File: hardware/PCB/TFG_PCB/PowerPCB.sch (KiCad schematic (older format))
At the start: 52 parts, among them J1 Conn_01x02_Male, J11 Conn_01x02_Male, J13 Conn_01x02_Male, J15 Conn_01x04_Male, J18 Conn_01x02_Male, J19 Conn_01x02_Male, J21 Conn_01x02_Male, J22 Conn_01x02_Male, J23 Conn_01x04_Male, J25 Conn_01x04_Male, J26 Conn_01x04_Male, J28 Conn_01x02_Male, J30 Conn_01x02_Male, J4 Conn_01x04_Male, J6 Conn_01x04_Male, J7 Conn_01x02_Male, J9 Conn_01x04_Male, Q1 IRF540N, Q4 FDD6685, Q6 FDD6685, Q8 2N7002, U2 L78L05_SOT89, U4 TD7590_2, U6 TD7590_2

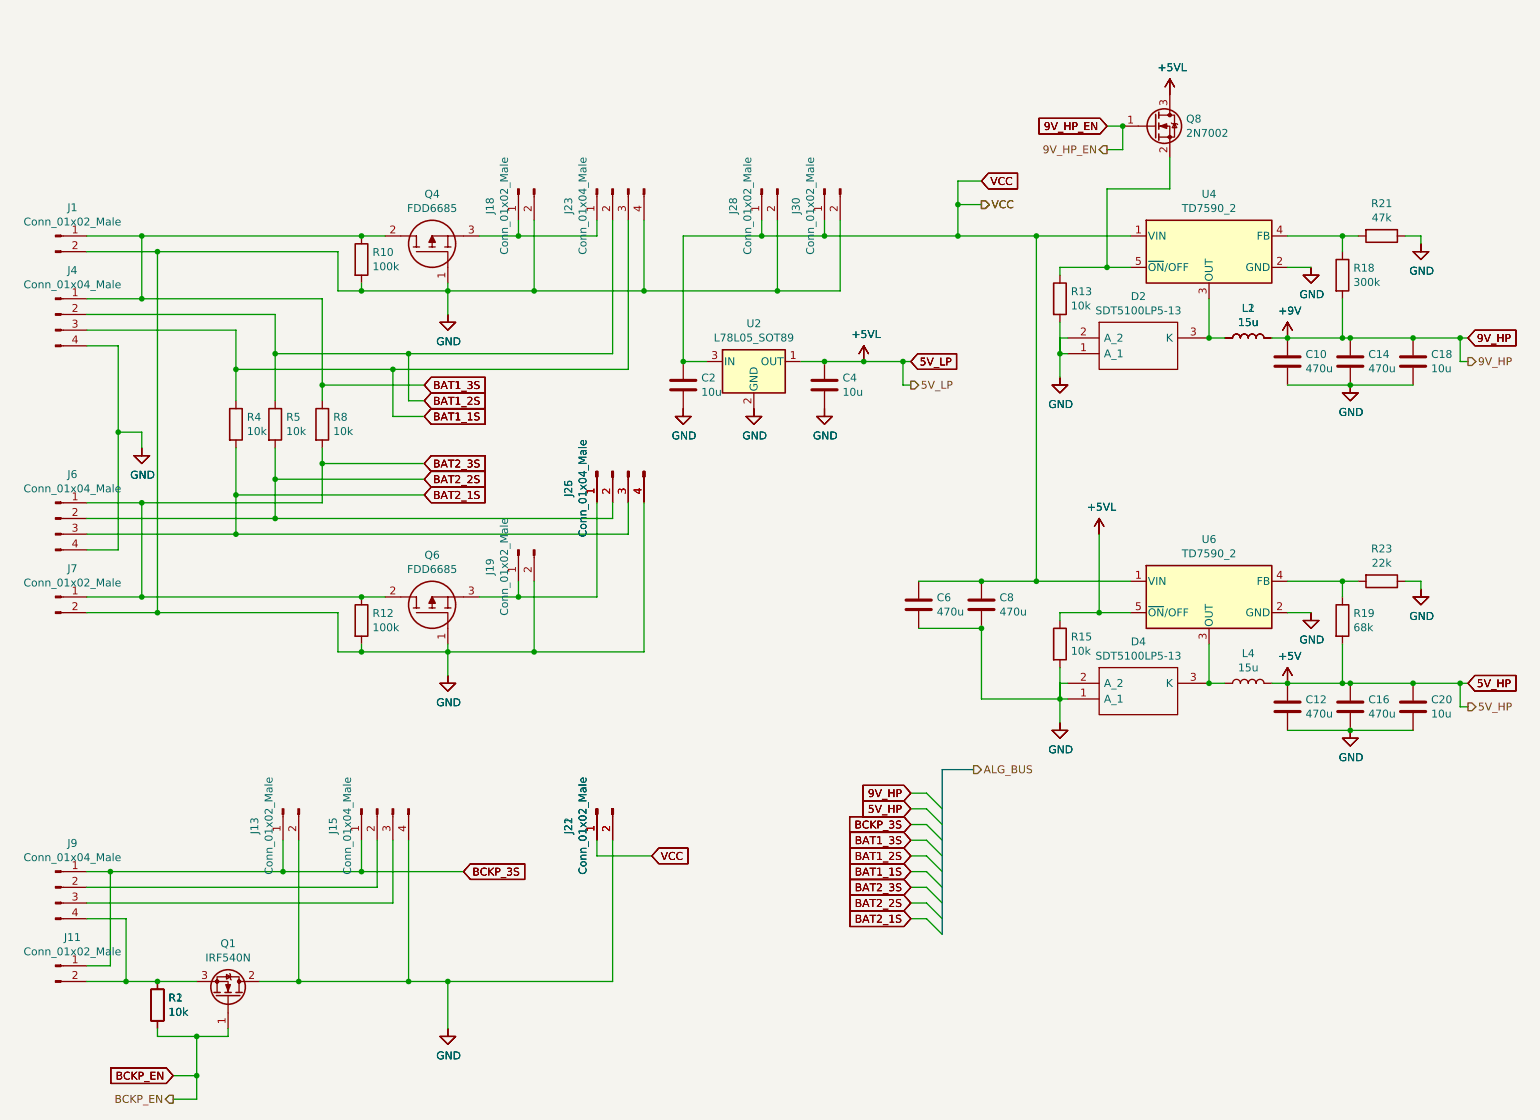
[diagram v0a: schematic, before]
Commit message: added footprints
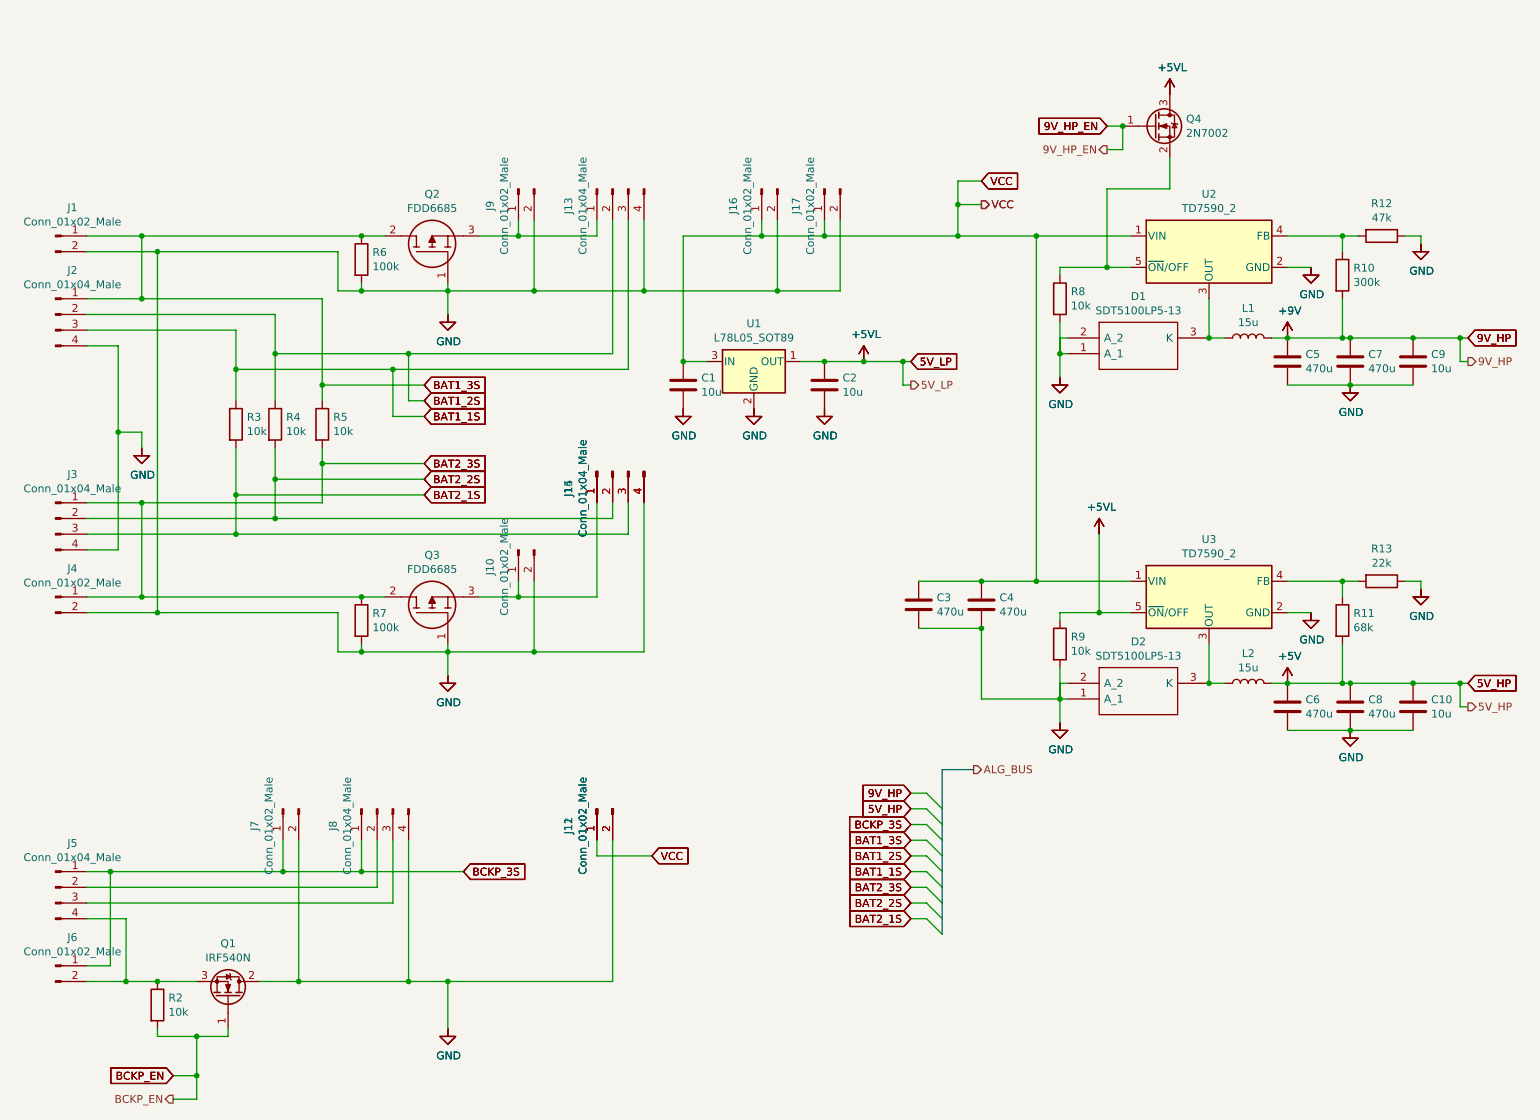
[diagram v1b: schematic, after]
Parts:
- removed L1: 15u, Inductor_SMD:L_0603_1608Metric, symbol Device:L
- removed R1: 10k, symbol Device:R
- C1: renamed from C2; footprint (none) -> Capacitor_SMD:C_2512_6332Metric_Pad1.52x3.35mm_HandSolder
- C2: renamed from C4; footprint (none) -> Capacitor_SMD:C_2512_6332Metric_Pad1.52x3.35mm_HandSolder
- renumbered C20 to C10, C6 to C3, C8 to C4, C10 to C5, C12 to C6, C14 to C7, C16 to C8, C18 to C9, D2 to D1, D4 to D2, J19 to J10, J21 to J11, J22 to J12, J23 to J13, J25 to J14, J26 to J15, J28 to J16, J30 to J17, J4 to J2, J6 to J3, J7 to J4, J9 to J5, J11 to J6, J13 to J7, J15 to J8, J18 to J9, L2 to L1, L4 to L2, Q4 to Q2, Q6 to Q3, Q8 to Q4, R18 to R10, R19 to R11, R21 to R12, R23 to R13, R4 to R3, R5 to R4, R8 to R5, R10 to R6, R12 to R7, R13 to R8, R15 to R9, U2 to U1, U4 to U2, U6 to U3

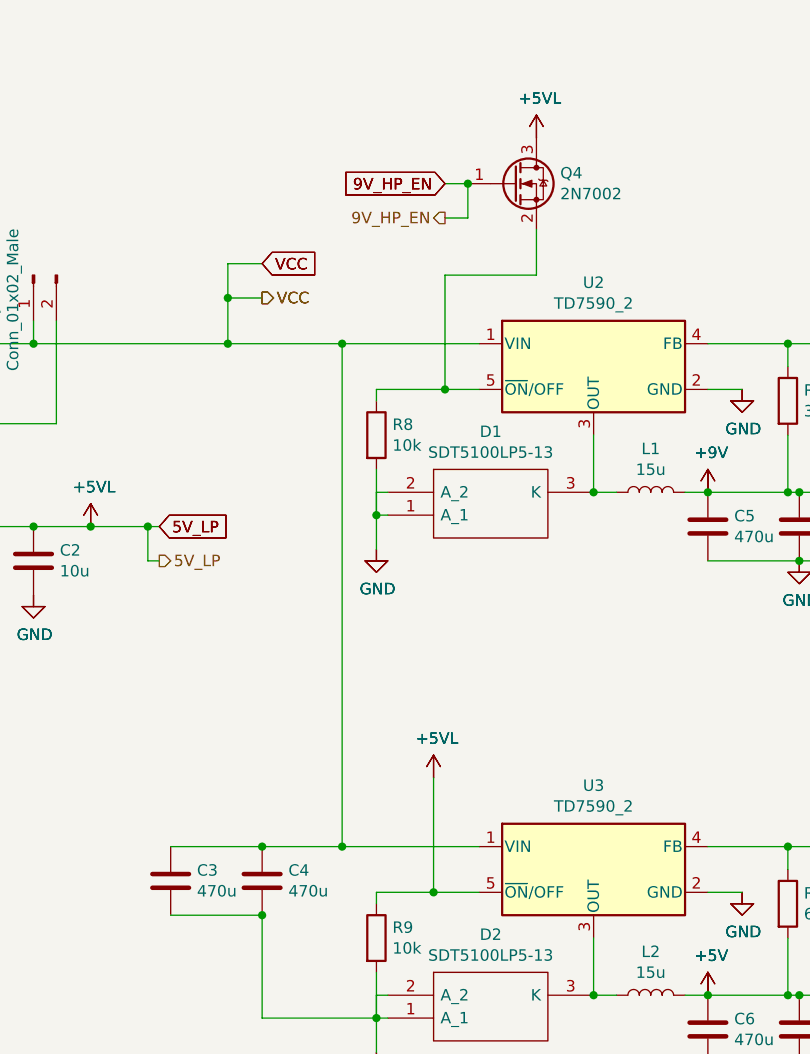
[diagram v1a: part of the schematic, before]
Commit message: netlist and Motor Control sheet
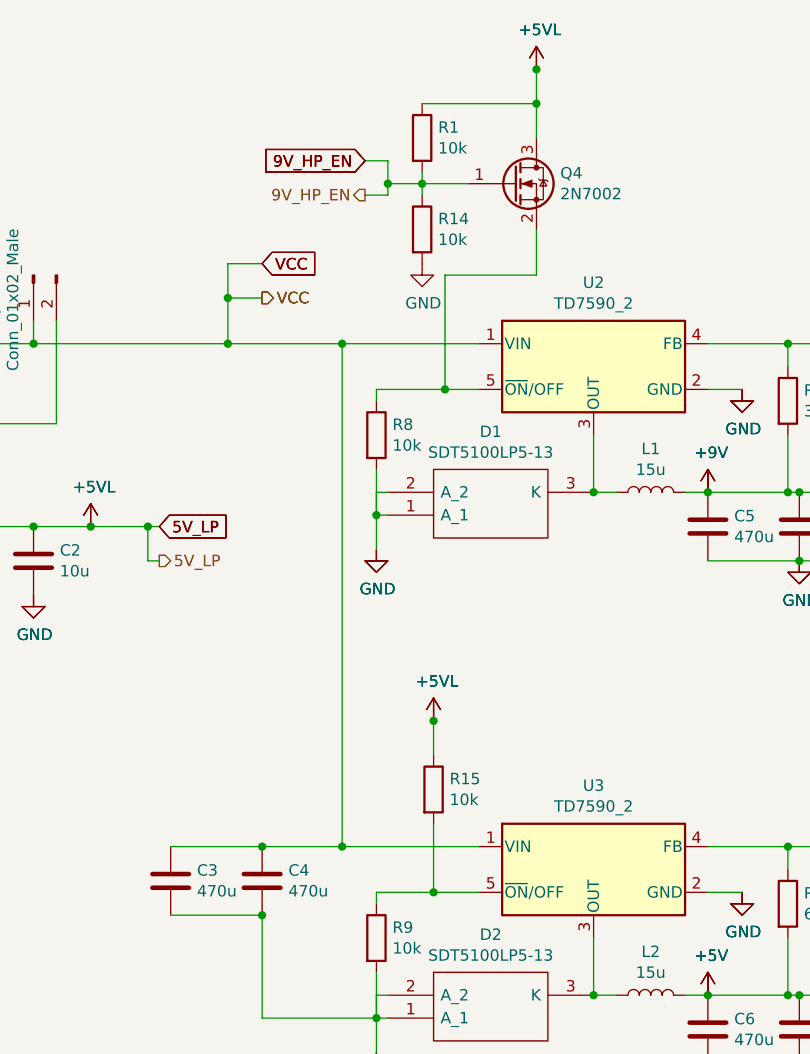
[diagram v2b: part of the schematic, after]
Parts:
- added R1, R14, R15: 10k, symbol Device:R
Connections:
- net +5VL: now also R1.1, R15.1; no longer R9.1, U3.5 (~ON~/OFF)
- net 9V_HP_EN: now also R1.2, R14.1
- net GND: now also R14.2
- new net: R15.2, R9.1, U3.5 (~ON~/OFF)
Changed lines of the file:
@@
 Wire Wire Line
 	8100 4350 8100 4300
-Wire Wire Line
-	8100 4300 8350 4300
 $Comp
 L power:+5VL #PWR?
 U 1 1 5E762A7A
-P 8800 1000
+P 8800 700
 AR Path="/5E762A7A" Ref="#PWR?"  Part="1"
 AR Path="/5E6BD4F2/5E762A7A" Ref="#PWR023"  Part="1"
-F 0 "#PWR023" H 8800 850 50  0001 C CNN
-F 1 "+5VL" H 8815 1173 50  0000 C CNN
-F 2 "" H 8800 1000 50  0001 C CNN
-F 3 "" H 8800 1000 50  0001 C CNN
-	1    8800 1000
+F 0 "#PWR023" H 8800 550 50  0001 C CNN
+F 1 "+5VL" H 8815 873 50  0000 C CNN
+F 2 "" H 8800 700 50  0001 C CNN
+F 3 "" H 8800 700 50  0001 C CNN
+	1    8800 700
 	1    0    0    -1
 $EndComp
@@
 L power:+5VL #PWR?
 U 1 1 5E762A80
-P 8350 3800
+P 8350 3550
 AR Path="/5E762A80" Ref="#PWR?"  Part="1"
 AR Path="/5E6BD4F2/5E762A80" Ref="#PWR021"  Part="1"
-F 0 "#PWR021" H 8350 3650 50  0001 C CNN
-F 1 "+5VL" H 8365 3973 50  0000 C CNN
-F 2 "" H 8350 3800 50  0001 C CNN
-F 3 "" H 8350 3800 50  0001 C CNN
-	1    8350 3800
+F 0 "#PWR021" H 8350 3400 50  0001 C CNN
+F 1 "+5VL" H 8365 3723 50  0000 C CNN
+F 2 "" H 8350 3550 50  0001 C CNN
+F 3 "" H 8350 3550 50  0001 C CNN
+	1    8350 3550
 	1    0    0    -1
 $EndComp
@@
 Wire Wire Line
 	8400 1600 8400 2100
-Connection ~ 8350 4300
-Wire Wire Line
-	8350 4300 8550 4300
-Wire Wire Line
-	8350 3800 8350 4300
-Text GLabel 8400 1200 0    50   Input ~ 0
+Text GLabel 8050 1100 0    50   Input ~ 0
 9V_HP_EN
 Wire Wire Line
-	8500 1200 8400 1200
+	8150 1100 8050 1100
 $Comp
 L power:GND #PWR?
@@
 $EndComp
 $Comp
-L Transistor_FET:2N7002 Q?
-U 1 1 5E97A733
-P 8700 1200
-AR Path="/5E97A733" Ref="Q?"  Part="1"
-AR Path="/5E6BD4F2/5E97A733" Ref="Q4"  Part="1"
-F 0 "Q4" H 8904 1246 50  0000 L CNN
-F 1 "2N7002" H 8904 1155 50  0000 L CNN
-F 2 "Package_TO_SOT_SMD:SOT-23" H 8900 1125 50  0001 L CIN
-F 3 "https://www.fairchildsemi.com/datasheets/2N/2N7002.pdf" H 8700 1200 50  0001 L CNN
-	1    8700 1200
-	1    0    0    -1
-$EndComp
-$Comp
 L power:+5VL #PWR?
 U 1 1 5E97A734
-P 8800 1000
+P 8800 700
 AR Path="/5E97A734" Ref="#PWR?"  Part="1"
 AR Path="/5E6BD4F2/5E97A734" Ref="#PWR024"  Part="1"
-F 0 "#PWR024" H 8800 850 50  0001 C CNN
-F 1 "+5VL" H 8815 1173 50  0000 C CNN
-F 2 "" H 8800 1000 50  0001 C CNN
-F 3 "" H 8800 1000 50  0001 C CNN
-	1    8800 1000
+F 0 "#PWR024" H 8800 550 50  0001 C CNN
+F 1 "+5VL" H 8815 873 50  0000 C CNN
+F 2 "" H 8800 700 50  0001 C CNN
+F 3 "" H 8800 700 50  0001 C CNN
+	1    8800 700
 	1    0    0    -1
 $EndComp
@@
 L power:+5VL #PWR?
 U 1 1 5E97A735
-P 8350 3800
+P 8350 3550
 AR Path="/5E97A735" Ref="#PWR?"  Part="1"
 AR Path="/5E6BD4F2/5E97A735" Ref="#PWR022"  Part="1"
-F 0 "#PWR022" H 8350 3650 50  0001 C CNN
-F 1 "+5VL" H 8365 3973 50  0000 C CNN
-F 2 "" H 8350 3800 50  0001 C CNN
-F 3 "" H 8350 3800 50  0001 C CNN
-	1    8350 3800
-	1    0    0    -1
-$EndComp
-Text GLabel 8400 1200 0    50   Input ~ 0
+F 0 "#PWR022" H 8350 3400 50  0001 C CNN
+F 1 "+5VL" H 8365 3723 50  0000 C CNN
+F 2 "" H 8350 3550 50  0001 C CNN
+F 3 "" H 8350 3550 50  0001 C CNN
+	1    8350 3550
+	1    0    0    -1
+$EndComp
+Text GLabel 8050 1100 0    50   Input ~ 0
 9V_HP_EN
 $Comp
@@
 	2600 7400 2600 7250
 Connection ~ 2600 7250
-Text HLabel 8400 1350 0    50   Output ~ 0
+Text HLabel 8050 1250 0    50   Output ~ 0
 9V_HP_EN
 Wire Wire Line
-	8400 1350 8500 1350
-Wire Wire Line
-	8500 1350 8500 1200
-Connection ~ 8500 1200
+	8050 1250 8150 1250
 Wire Wire Line
 	6600 1900 7450 1900
@@
 Wire Wire Line
 	7250 5450 7150 5450
+$Comp
+L Transistor_FET:2N7002 Q?
+U 1 1 5E97A733
+P 8700 1200
+AR Path="/5E97A733" Ref="Q?"  Part="1"
+AR Path="/5E6BD4F2/5E97A733" Ref="Q4"  Part="1"
+F 0 "Q4" H 8904 1246 50  0000 L CNN
+F 1 "2N7002" H 8904 1155 50  0000 L CNN
+F 2 "Package_TO_SOT_SMD:SOT-23" H 8900 1125 50  0001 L CIN
+F 3 "https://www.fairchildsemi.com/datasheets/2N/2N7002.pdf" H 8700 1200 50  0001 L CNN
+	1    8700 1200
+	1    0    0    -1
+$EndComp
+$Comp
+L Device:R R?
+U 1 1 5E586C94
+P 8300 1400
+AR Path="/5E586C94" Ref="R?"  Part="1"
+AR Path="/5E6BD4F2/5E586C94" Ref="R14"  Part="1"
+F 0 "R14" H 8370 1446 50  0000 L CNN
+F 1 "10k" H 8370 1355 50  0000 L CNN
+F 2 "" V 8230 1400 50  0001 C CNN
+F 3 "~" H 8300 1400 50  0001 C CNN
+	1    8300 1400
+	1    0    0    -1
+$EndComp
+$Comp
+L Device:R R?
+U 1 1 5E588A0C
+P 8300 1000
+AR Path="/5E588A0C" Ref="R?"  Part="1"
+AR Path="/5E6BD4F2/5E588A0C" Ref="R1"  Part="1"
+F 0 "R1" H 8370 1046 50  0000 L CNN
+F 1 "10k" H 8370 955 50  0000 L CNN
+F 2 "" V 8230 1000 50  0001 C CNN
+F 3 "~" H 8300 1000 50  0001 C CNN
+	1    8300 1000
+	1    0    0    -1
+$EndComp
+Wire Wire Line
+	8300 850  8800 850
+Wire Wire Line
+	8800 850  8800 700
+Connection ~ 8800 700
+Wire Wire Line
+	8800 850  8800 1000
+Connection ~ 8800 850
+Wire Wire Line
+	8300 1250 8300 1200
+Wire Wire Line
+	8500 1200 8300 1200
+Connection ~ 8300 1200
+Wire Wire Line
+	8300 1200 8300 1150
+Wire Wire Line
+	8150 1100 8150 1200
+Wire Wire Line
+	8300 1200 8150 1200
+Connection ~ 8150 1200
+Wire Wire Line
+	8150 1200 8150 1250
+$Comp
+L power:GND #PWR?
+U 1 1 5E5E2DD3
+P 8300 1550
+AR Path="/5E5E2DD3" Ref="#PWR?"  Part="1"
+AR Path="/5E6BD4F2/5E5E2DD3" Ref="#PWR0101"  Part="1"
+F 0 "#PWR0101" H 8300 1300 50  0001 C CNN
+F 1 "GND" H 8305 1377 50  0000 C CNN
+F 2 "" H 8300 1550 50  0001 C CNN
+F 3 "" H 8300 1550 50  0001 C CNN
+	1    8300 1550
+	1    0    0    -1
+$EndComp
+$Comp
+L Device:R R?
+U 1 1 5E5FD2A2
+P 8350 3850
+AR Path="/5E5FD2A2" Ref="R?"  Part="1"
+AR Path="/5E6BD4F2/5E5FD2A2" Ref="R15"  Part="1"
+F 0 "R15" H 8420 3896 50  0000 L CNN
+F 1 "10k" H 8420 3805 50  0000 L CNN
+F 2 "" V 8280 3850 50  0001 C CNN
+F 3 "~" H 8350 3850 50  0001 C CNN
+	1    8350 3850
+	1    0    0    -1
+$EndComp
+Wire Wire Line
+	8350 3700 8350 3550
+Connection ~ 8350 3550
+Wire Wire Line
+	8350 4000 8350 4300
+Wire Wire Line
+	8100 4300 8350 4300
+Connection ~ 8350 4300
+Wire Wire Line
+	8350 4300 8550 4300
 Wire Bus Line
 	7350 5300 7350 6350
